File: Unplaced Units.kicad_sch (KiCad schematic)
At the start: 2 parts, among them SW2 SW_DPDT_x2, U4 LM339

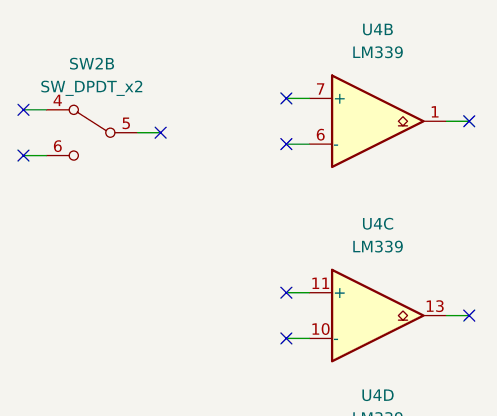
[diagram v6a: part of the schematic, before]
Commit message: Removed the two LED indicators
Removed the two LED indicators for each power source and replaced them with a single LED for the final 5V rail
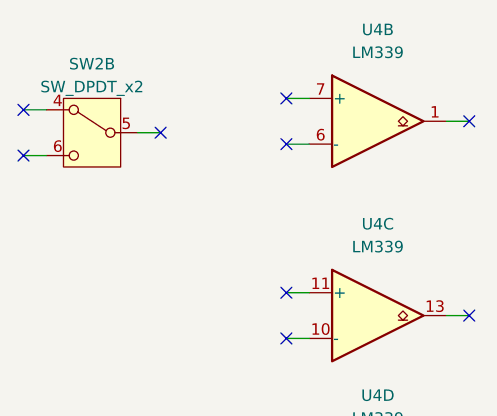
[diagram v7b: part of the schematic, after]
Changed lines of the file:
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@@
 	(title_block
 		(title "ATMEGA32A AVR Kit")
-		(date "2023-12-08")
-		(rev "C1")
+		(date "2024-06-14")
+		(rev "C2.7")
 		(company "Team Exotic")
 		(comment 1 "Author: Morad Tamer")
@@
 			)
 		)
-		(property "Description" ""
+		(property "Description" "Switch, dual pole double throw, separate symbols"
 			(at 30.48 34.29 0)
 			(effects
